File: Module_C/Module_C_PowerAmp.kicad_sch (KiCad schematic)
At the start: 30 parts, among them J1 Audio_In_Molex_KK, J2 Speaker_Screw_Term, J3 PWR_32V_Molex_KK, J4 PWR_12V_Molex_KK, U1 NE5532

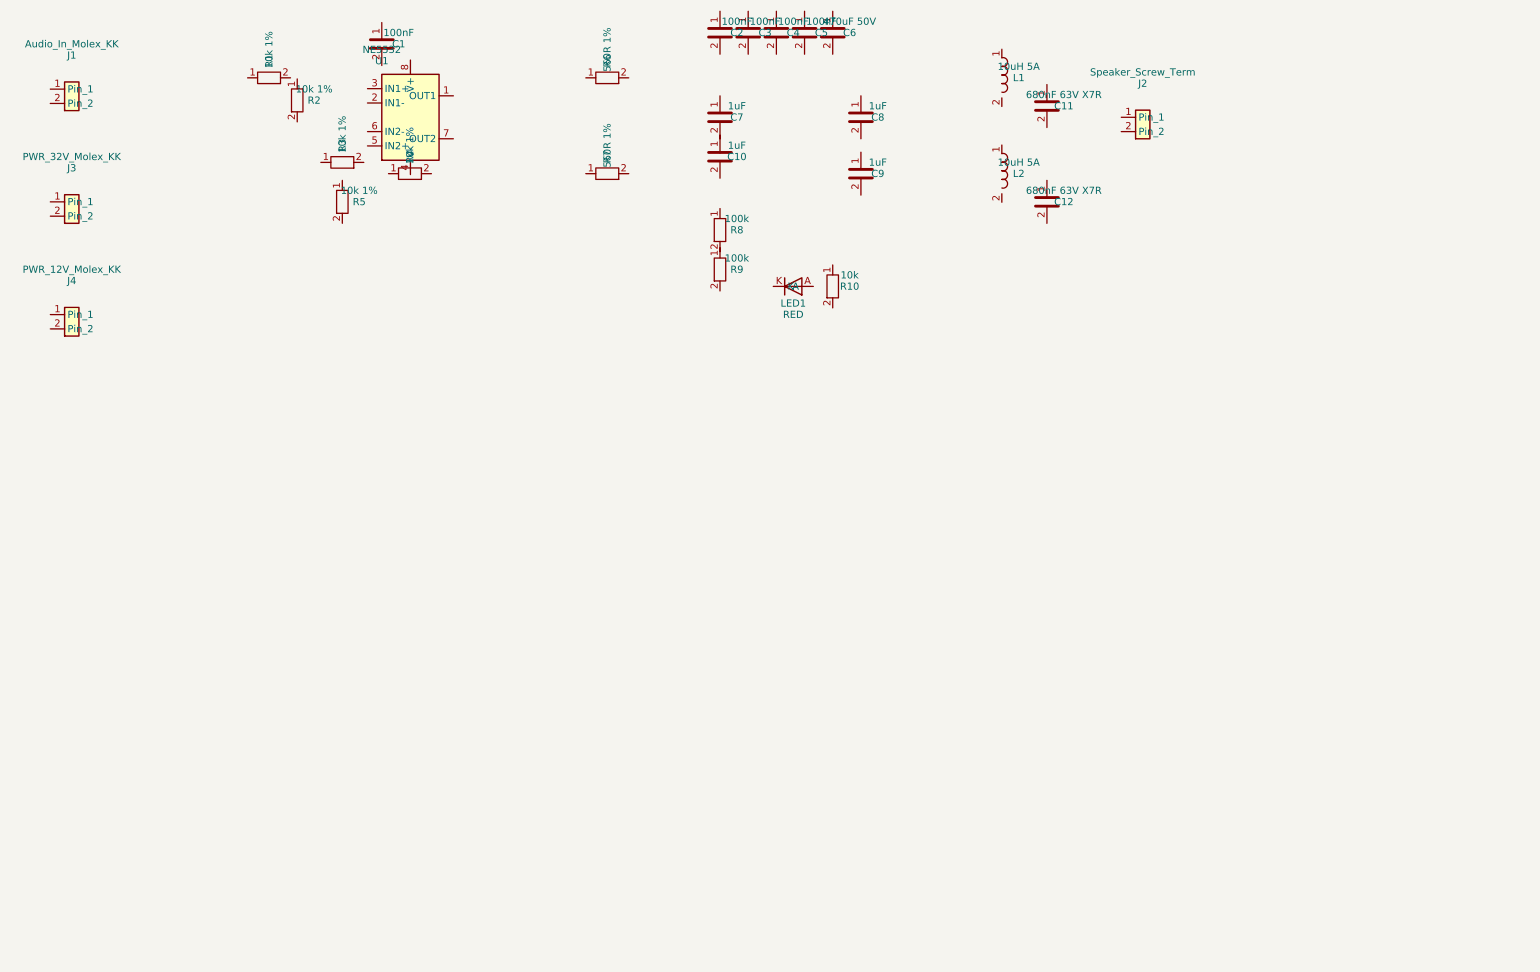
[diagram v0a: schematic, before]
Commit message: Add U1 NE5532 and U2 TPA3251 placed
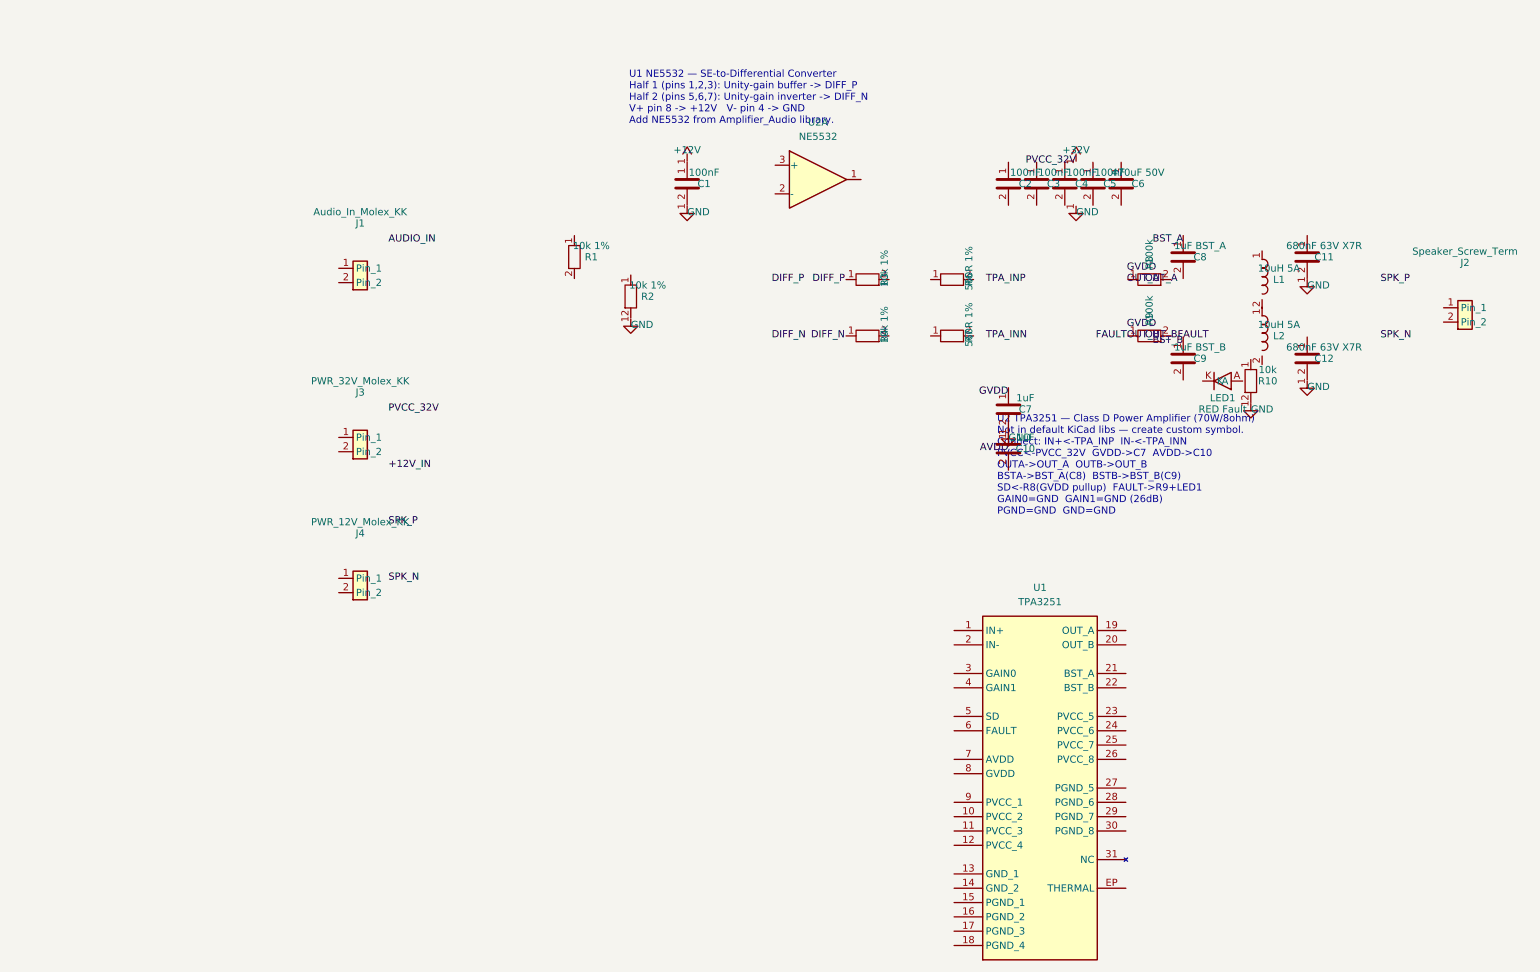
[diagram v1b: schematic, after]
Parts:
- removed R5: 10k 1%, symbol Device:R
- removed U1: NE5532, symbol Amplifier_Audio:NE5532
- added U1: TPA3251, Package_QFP:HTQFP-48_7x7mm_P0.5mm, symbol TPA3251:TPA3251
- added U2: NE5532, symbol Amplifier_Operational:NE5532
- C8: value 1uF -> 1uF BST_A
- C9: value 1uF -> 1uF BST_B
- J1, J3, J4: footprint (none) -> Connector_Molex:Molex_KK-254_AE-6410-02A_1x02_P2.54mm_Vertical
- J2: footprint (none) -> Connector_Phoenix_MKDS:PhoenixContact_MKDS_1,5_2-5.08_1x02_P5.08mm_Vertical
- L1, L2: footprint (none) -> Inductor_SMD:L_Bourns_SRR1260
- LED1: value RED -> RED Fault
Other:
- note added: "U1 NE5532 — SE-to-Differential Converter Half 1 (pins 1,2,3): Unity-gain buffer -> DIFF_P Half 2 (pins 5,6,7): Unity-gain inverter -> DIFF_N V+ pin 8 -> +12V V- pin 4 -> GND Add NE5532 from Amplifier_Audio library."
- note added: "U2 TPA3251 — Class D Power Amplifier (70W/8ohm) Not in default KiCad libs — create custom symbol. Connect: IN+<-TPA_INP IN-<-TPA_INN PVCC<-PVCC_32V GVDD->C7 AVDD->C10 OUTA->OUT_A OUTB->OUT_B BSTA->BST_A(C8) BSTB->BST_B(C9) SD<-R8(GVDD pullup) FAULT->R9+LED1 GAIN0=GND GAIN1=GND (26dB) PGND=GND GND=GND"
- company: (none) -> KiCad-Claude
- title: (none) -> Module C — Power Amplifier
